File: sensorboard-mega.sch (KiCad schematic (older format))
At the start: 14 parts, among them P1 Digital, P10 CONN_01X01, P11 CONN_01X01, P12 CONN_01X01, P13 CONN_01X01, P2 Power, P3 Analog, P4 Analog, P5 PWM, P6 PWM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

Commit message: Add level converters for SPI and I2C busses
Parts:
- added U? (x2): Level_Converter, symbol New_Library:Level_Converter
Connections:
- net +3V3: now also U?.10 (LV), U?.10 (LV)
- net +5V: now also U?.3 (HV), U?.3 (HV)
- net 10(**): now also U?.6 (HV1)
- net 20(SDA): now also U?.1 (HV4)
- net 21(SCL): now also U?.2 (HV3)
- net 50(MISO): now also U?.1 (HV4)
- net 51(MOSI): now also U?.2 (HV3)
- net 52(SCK): now also U?.5 (HV2)
- net GND: now also U?.4 (GND), U?.4 (GND), U?.9 (GND), U?.9 (GND)
- new net 3v3_MISO: U?.12 (LV4)
- new net 3v3_MOSI: U?.11 (LV3)
- new net 3v3_SCK: U?.8 (LV2)
- new net 3v3_SCL: U?.11 (LV3)
- new net 3v3_SDA: U?.12 (LV4)
- new net 3v3_SS: U?.7 (LV1)
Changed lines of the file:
@@
 Text Label 9300 6250 0    50   ~ 0
 52(SCK)
-Text Label 10050 6250 0    50   ~ 0
+Text Label 10350 6250 0    50   ~ 0
 51(MOSI)
 Text Label 9300 6350 0    50   ~ 0
 Reset
+Text Label 1100 3000 0    50   ~ 0
+50(MISO)
+Text Label 1100 3100 0    50   ~ 0
+51(MOSI)
+Text Label 1100 3400 0    50   ~ 0
+52(SCK)
+Text Label 1100 3500 0    60   ~ 0
+10(**)
+Wire Wire Line
+	1100 3500 1400 3500
+Wire Wire Line
+	1400 3400 1100 3400
+Wire Wire Line
+	1100 3100 1400 3100
+Wire Wire Line
+	1400 3000 1100 3000
+$Comp
+L New_Library:Level_Converter U?
+U 1 1 5DEE3BFA
+P 1700 2750
+F 0 "U?" H 1700 2765 50  0000 C CNN
+F 1 "Level_Converter" H 1700 2674 50  0000 C CNN
+F 2 "" H 1700 2750 50  0001 C CNN
+F 3 "" H 1700 2750 50  0001 C CNN
+	1    1700 2750
+	1    0    0    -1
+$EndComp
+Text Label 2200 3500 0    50   ~ 0
+3v3_SS
+Text Label 2200 3400 0    50   ~ 0
+3v3_SCK
+Text Label 2200 3100 0    50   ~ 0
+3v3_MOSI
+Text Label 2200 3000 0    50   ~ 0
+3v3_MISO
+Wire Wire Line
+	2000 3000 2200 3000
+Wire Wire Line
+	2000 3100 2200 3100
+Wire Wire Line
+	2000 3400 2200 3400
+Wire Wire Line
+	2000 3500 2200 3500
+Wire Wire Line
+	1400 3200 900  3200
+Wire Wire Line
+	900  3200 900  2900
+Wire Wire Line
+	1400 3300 900  3300
+Wire Wire Line
+	900  3300 900  3700
+Wire Wire Line
+	2700 3300 2700 3700
+Wire Wire Line
+	2000 3300 2700 3300
+Wire Wire Line
+	2000 3200 2700 3200
+Wire Wire Line
+	2700 3200 2700 2900
+$Comp
+L power:GND #PWR?
+U 1 1 5DF6CA90
+P 900 3700
+F 0 "#PWR?" H 900 3450 50  0001 C CNN
+F 1 "GND" H 905 3527 50  0000 C CNN
+F 2 "" H 900 3700 50  0001 C CNN
+F 3 "" H 900 3700 50  0001 C CNN
+	1    900  3700
+	1    0    0    -1
+$EndComp
+$Comp
+L power:GND #PWR?
+U 1 1 5DF6CD61
+P 2700 3700
+F 0 "#PWR?" H 2700 3450 50  0001 C CNN
+F 1 "GND" H 2705 3527 50  0000 C CNN
+F 2 "" H 2700 3700 50  0001 C CNN
+F 3 "" H 2700 3700 50  0001 C CNN
+	1    2700 3700
+	1    0    0    -1
+$EndComp
+$Comp
+L power:+5V #PWR?
+U 1 1 5DF6D2BB
+P 900 2900
+F 0 "#PWR?" H 900 2750 50  0001 C CNN
+F 1 "+5V" H 915 3073 50  0000 C CNN
+F 2 "" H 900 2900 50  0001 C CNN
+F 3 "" H 900 2900 50  0001 C CNN
+	1    900  2900
+	1    0    0    -1
+$EndComp
+$Comp
+L power:+3V3 #PWR?
+U 1 1 5DF6D689
+P 2700 2900
+F 0 "#PWR?" H 2700 2750 50  0001 C CNN
+F 1 "+3V3" H 2715 3073 50  0000 C CNN
+F 2 "" H 2700 2900 50  0001 C CNN
+F 3 "" H 2700 2900 50  0001 C CNN
+	1    2700 2900
+	1    0    0    -1
+$EndComp
+Text Label 1100 4400 0    50   ~ 0
+20(SDA)
+Text Label 1100 4500 0    50   ~ 0
+21(SCL)
+Wire Wire Line
+	1100 4500 1400 4500
+Wire Wire Line
+	1400 4400 1100 4400
+$Comp
+L New_Library:Level_Converter U?
+U 1 1 5DF6F05E
+P 1700 4150
+F 0 "U?" H 1700 4165 50  0000 C CNN
+F 1 "Level_Converter" H 1700 4074 50  0000 C CNN
+F 2 "" H 1700 4150 50  0001 C CNN
+F 3 "" H 1700 4150 50  0001 C CNN
+	1    1700 4150
+	1    0    0    -1
+$EndComp
+Text Label 2200 4500 0    50   ~ 0
+3v3_SCL
+Text Label 2200 4400 0    50   ~ 0
+3v3_SDA
+Wire Wire Line
+	2000 4400 2200 4400
+Wire Wire Line
+	2000 4500 2200 4500
+Wire Wire Line
+	1400 4600 900  4600
+Wire Wire Line
+	900  4600 900  4300
+Wire Wire Line
+	1400 4700 900  4700
+Wire Wire Line
+	900  4700 900  5100
+Wire Wire Line
+	2700 4700 2700 5100
+Wire Wire Line
+	2000 4700 2700 4700
+Wire Wire Line
+	2000 4600 2700 4600
+Wire Wire Line
+	2700 4600 2700 4300
+$Comp
+L power:GND #PWR?
+U 1 1 5DF6F074
+P 900 5100
+F 0 "#PWR?" H 900 4850 50  0001 C CNN
+F 1 "GND" H 905 4927 50  0000 C CNN
+F 2 "" H 900 5100 50  0001 C CNN
+F 3 "" H 900 5100 50  0001 C CNN
+	1    900  5100
+	1    0    0    -1
+$EndComp
+$Comp
+L power:GND #PWR?
+U 1 1 5DF6F07A
+P 2700 5100
+F 0 "#PWR?" H 2700 4850 50  0001 C CNN
+F 1 "GND" H 2705 4927 50  0000 C CNN
+F 2 "" H 2700 5100 50  0001 C CNN
+F 3 "" H 2700 5100 50  0001 C CNN
+	1    2700 5100
+	1    0    0    -1
+$EndComp
+$Comp
+L power:+5V #PWR?
+U 1 1 5DF6F080
+P 900 4300
+F 0 "#PWR?" H 900 4150 50  0001 C CNN
+F 1 "+5V" H 915 4473 50  0000 C CNN
+F 2 "" H 900 4300 50  0001 C CNN
+F 3 "" H 900 4300 50  0001 C CNN
+	1    900  4300
+	1    0    0    -1
+$EndComp
+$Comp
+L power:+3V3 #PWR?
+U 1 1 5DF6F086
+P 2700 4300
+F 0 "#PWR?" H 2700 4150 50  0001 C CNN
+F 1 "+3V3" H 2715 4473 50  0000 C CNN
+F 2 "" H 2700 4300 50  0001 C CNN
+F 3 "" H 2700 4300 50  0001 C CNN
+	1    2700 4300
+	1    0    0    -1
+$EndComp
 $EndSCHEMATC

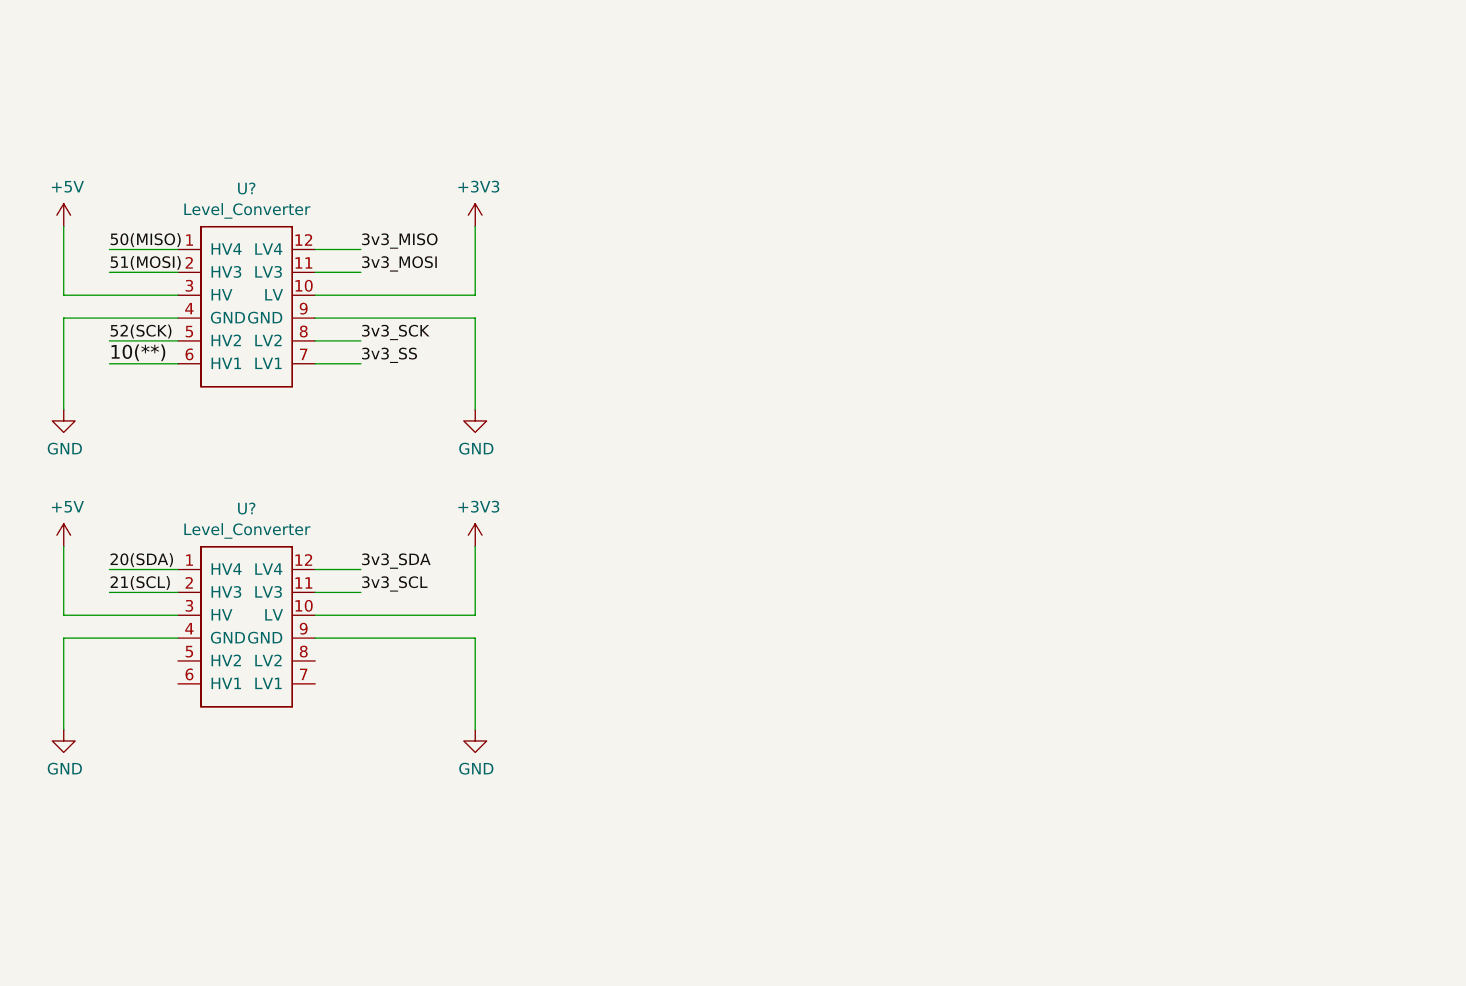
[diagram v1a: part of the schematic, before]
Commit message: Add internal DHT22 sensor
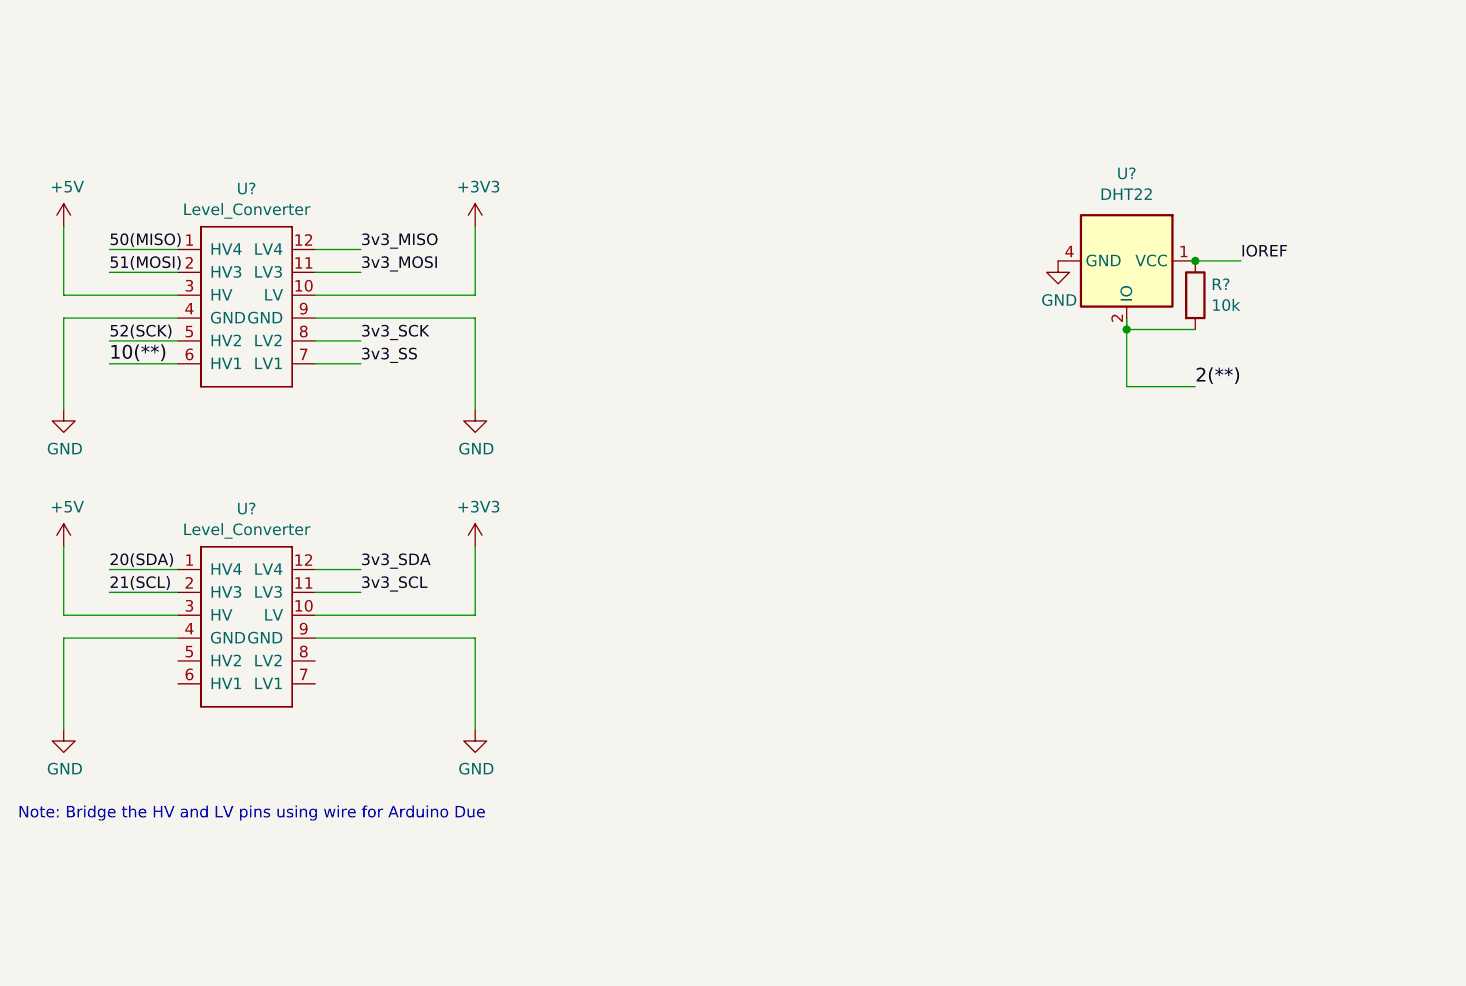
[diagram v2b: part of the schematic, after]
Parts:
- added R?: 10k, symbol Device:R
- added U?: DHT22, Sensor:Aosong_DHT11_5.5x12.0_P2.54mm, symbol Sensor:DHT22
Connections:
- net 2(**): now also R?.2, U?.2 (IO)
- net GND: now also U?.4 (GND)
- net IOREF: now also R?.1, U?.1 (VCC)
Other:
- note added: "Note: Bridge the HV and LV pins using wire for Arduino Due"
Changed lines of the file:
@@
 	1    0    0    -1
 $EndComp
+Wire Wire Line
+	5850 3050 6050 3050
+Text Label 6050 3050 0    50   ~ 0
+IOREF
+$Comp
+L Device:R R?
+U 1 1 5DF91E75
+P 5850 3200
+F 0 "R?" H 5920 3246 50  0000 L CNN
+F 1 "10k" H 5920 3155 50  0000 L CNN
+F 2 "" V 5780 3200 50  0001 C CNN
+F 3 "~" H 5850 3200 50  0001 C CNN
+	1    5850 3200
+	1    0    0    -1
+$EndComp
+Wire Wire Line
+	5850 3350 5550 3350
+$Comp
+L power:GND #PWR?
+U 1 1 5DF988E0
+P 5250 3050
+F 0 "#PWR?" H 5250 2800 50  0001 C CNN
+F 1 "GND" H 5255 2877 50  0000 C CNN
+F 2 "" H 5250 3050 50  0001 C CNN
+F 3 "" H 5250 3050 50  0001 C CNN
+	1    5250 3050
+	1    0    0    -1
+$EndComp
+$Comp
+L Sensor:DHT22 U?
+U 1 1 5DF9B2BC
+P 5550 3050
+F 0 "U?" V 5169 3050 50  0000 C CNN
+F 1 "DHT22" V 5260 3050 50  0000 C CNN
+F 2 "Sensor:Aosong_DHT11_5.5x12.0_P2.54mm" H 5550 2650 50  0001 C CNN
+F 3 "http://akizukidenshi.com/download/ds/aosong/DHT11.pdf" H 5700 3300 50  0001 C CNN
+	1    5550 3050
+	0    1    1    0
+$EndComp
+Connection ~ 5850 3050
+Text Notes 700  5500 0    50   ~ 0
+Note: Bridge the HV and LV pins using wire for Arduino Due
+Wire Wire Line
+	5550 3300 5550 3350
+Connection ~ 5550 3350
+Wire Wire Line
+	5550 3350 5550 3600
+Wire Wire Line
+	5550 3600 5850 3600
+Text Label 5850 3600 0    60   ~ 0
+2(**)
 $EndSCHEMATC

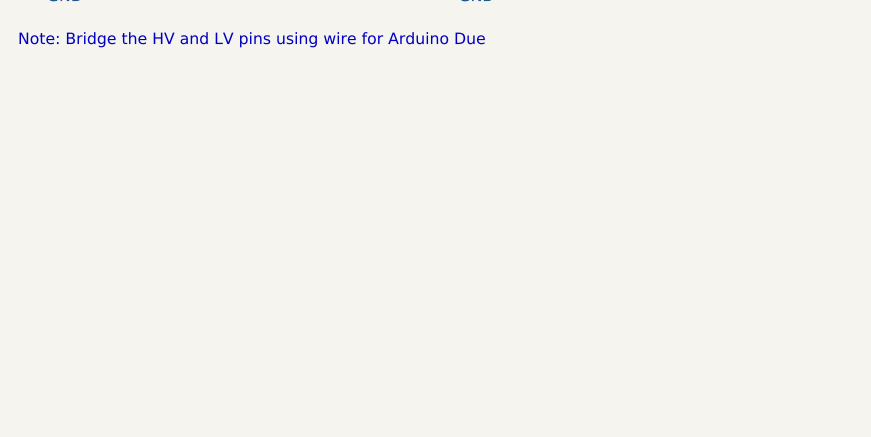
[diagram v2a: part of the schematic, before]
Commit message: Add SD card breakout board
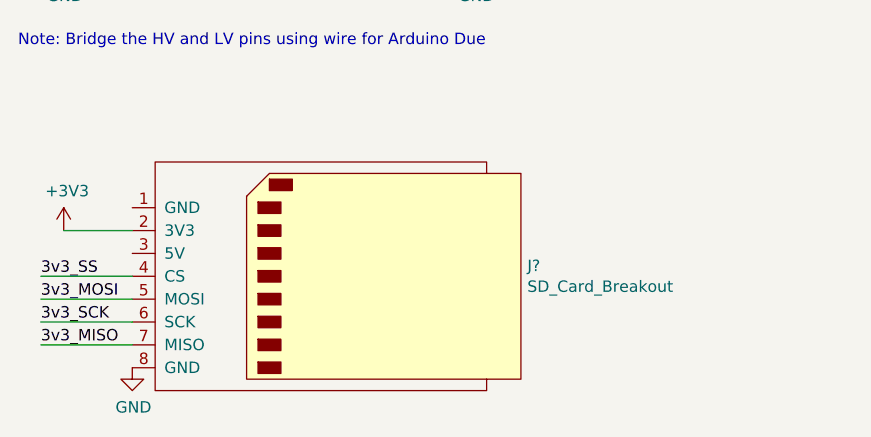
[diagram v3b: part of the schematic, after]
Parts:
- added J?: SD_Card_Breakout, symbol New_Library:SD_Card_Breakout
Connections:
- net +3V3: now also J?.2 (3V3)
- net 3v3_MISO: now also J?.7 (MISO)
- net 3v3_MOSI: now also J?.5 (MOSI)
- net 3v3_SCK: now also J?.6 (SCK)
- net 3v3_SS: now also J?.4 (CS)
- net GND: now also J?.8 (GND)
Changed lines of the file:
@@
 Text Label 5850 3600 0    60   ~ 0
 2(**)
+$Comp
+L New_Library:SD_Card_Breakout J?
+U 1 1 5DFE5C2E
+P 2100 6500
+F 0 "J?" H 2928 6546 50  0000 L CNN
+F 1 "SD_Card_Breakout" H 2928 6455 50  0000 L CNN
+F 2 "" H 2100 6500 50  0001 C CNN
+F 3 "http://portal.fciconnect.com/Comergent//fci/drawing/10067847.pdf" H 2100 6500 50  0001 C CNN
+	1    2100 6500
+	1    0    0    -1
+$EndComp
+$Comp
+L power:GND #PWR?
+U 1 1 5DFF28AA
+P 1200 6900
+F 0 "#PWR?" H 1200 6650 50  0001 C CNN
+F 1 "GND" H 1205 6727 50  0000 C CNN
+F 2 "" H 1200 6900 50  0001 C CNN
+F 3 "" H 1200 6900 50  0001 C CNN
+	1    1200 6900
+	1    0    0    -1
+$EndComp
+$Comp
+L power:+3V3 #PWR?
+U 1 1 5DFF2EFF
+P 900 6300
+F 0 "#PWR?" H 900 6150 50  0001 C CNN
+F 1 "+3V3" H 915 6473 50  0000 C CNN
+F 2 "" H 900 6300 50  0001 C CNN
+F 3 "" H 900 6300 50  0001 C CNN
+	1    900  6300
+	1    0    0    -1
+$EndComp
+Wire Wire Line
+	900  6300 1200 6300
+Wire Wire Line
+	800  6500 1200 6500
+Wire Wire Line
+	800  6600 1200 6600
+Wire Wire Line
+	800  6700 1200 6700
+Wire Wire Line
+	800  6800 1200 6800
+Text Label 800  6800 0    50   ~ 0
+3v3_MISO
+Text Label 800  6600 0    50   ~ 0
+3v3_MOSI
+Text Label 800  6700 0    50   ~ 0
+3v3_SCK
+Text Label 800  6500 0    50   ~ 0
+3v3_SS
 $EndSCHEMATC

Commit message: Change description
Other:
- note added: "Note: Bridge the HV and LV signal pins using wire for Arduino Due"
- note removed: "Note: Bridge the HV and LV pins using wire for Arduino Due"
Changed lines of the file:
@@
 Connection ~ 5850 3050
 Text Notes 700  5500 0    50   ~ 0
-Note: Bridge the HV and LV pins using wire for Arduino Due
+Note: Bridge the HV and LV signal pins using wire for Arduino Due
 Wire Wire Line
 	5550 3300 5550 3350

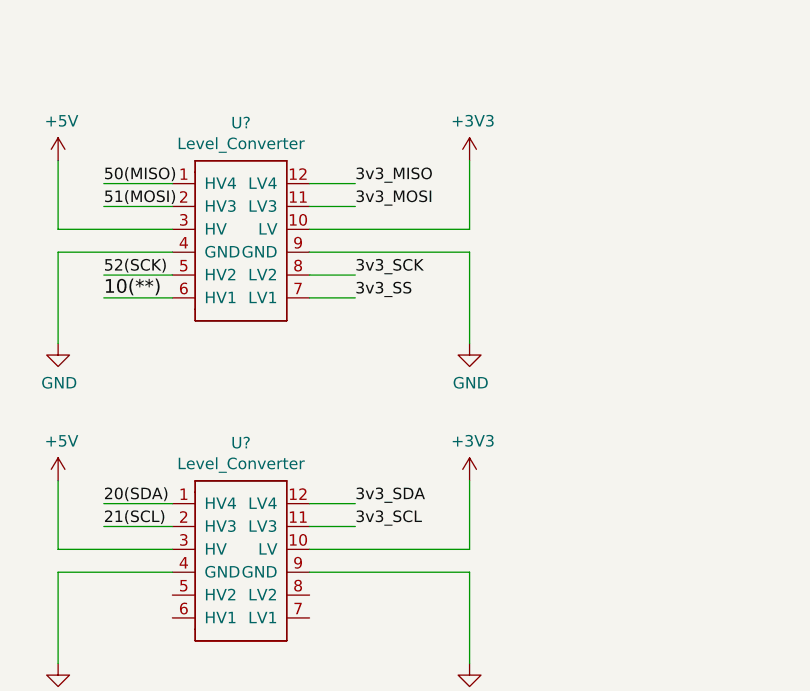
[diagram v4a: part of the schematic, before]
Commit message: Rename 3v3 nets to 3V3
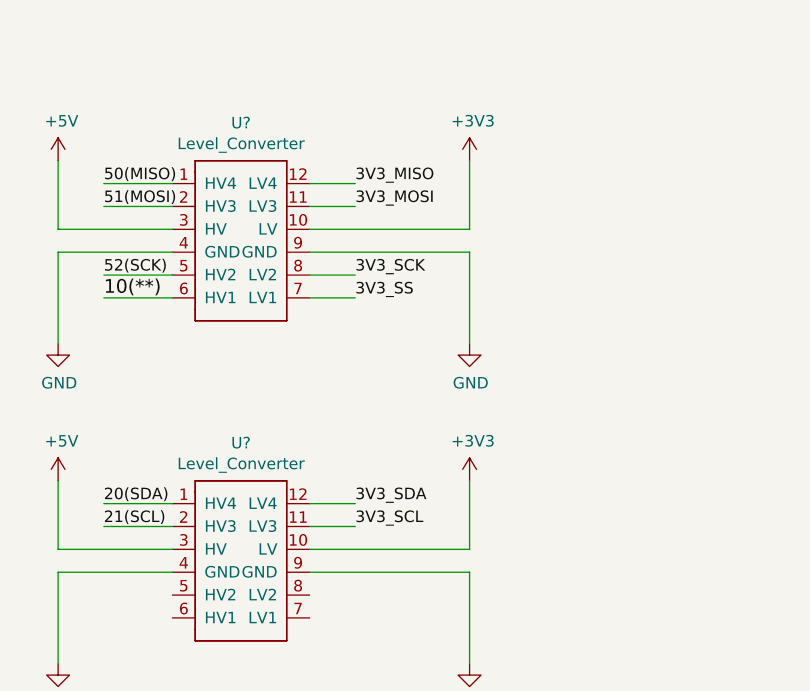
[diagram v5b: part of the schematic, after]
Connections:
- net 3v3_MISO: no longer U?.12 (LV4)
- net 3v3_MOSI: no longer U?.11 (LV3)
- net 3v3_SCK: no longer U?.8 (LV2)
- net 3v3_SS: no longer U?.7 (LV1)
- net 3v3_SCL renamed 3V3_SCL
- net 3v3_SDA renamed 3V3_SDA
- new net 3V3_MISO: U?.12 (LV4)
- new net 3V3_MOSI: U?.11 (LV3)
- new net 3V3_SCK: U?.8 (LV2)
- new net 3V3_SS: U?.7 (LV1)
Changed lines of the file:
@@
 $EndComp
 Text Label 2200 3500 0    50   ~ 0
-3v3_SS
+3V3_SS
 Text Label 2200 3400 0    50   ~ 0
-3v3_SCK
+3V3_SCK
 Text Label 2200 3100 0    50   ~ 0
-3v3_MOSI
+3V3_MOSI
 Text Label 2200 3000 0    50   ~ 0
-3v3_MISO
+3V3_MISO
 Wire Wire Line
 	2000 3000 2200 3000
@@
 $EndComp
 Text Label 2200 4500 0    50   ~ 0
-3v3_SCL
+3V3_SCL
 Text Label 2200 4400 0    50   ~ 0
-3v3_SDA
+3V3_SDA
 Wire Wire Line
 	2000 4400 2200 4400
